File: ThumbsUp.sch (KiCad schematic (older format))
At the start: 165 parts, among them IC1 RP2040, IC2 W25Q128JVSIM, IC3 RP2040, IC4 W25Q128JVSIM, J1 Conn_01x04_Male, J10 Raiser_Male, J11 Raiser_Female, J12 Raiser_Male, J13 Raiser_Female, J14 Raiser_Male, J15 Raiser_Female, J16 Raiser_Male, J17 Raiser_Female, J18 Raiser_Male, J19 Raiser_Female, J2 Conn_01x04_Male, J20 Conn_01x04_Female, J21 Conn_01x04_Female, J22 Conn_01x04_Female, J23 Conn_01x04_Female, J24 Conn_01x04_Male, J25 Conn_01x04_Male, J26 Conn_01x04_Male, J27 Conn_01x04_Male, J28 Conn_01x04_Female, J29 Conn_01x04_Female, J3 Conn_01x04_Female, J30 Conn_01x04_Female, J31 Conn_01x04_Female, J32 USB_C_Receptacle_USB2.0, J33 Raiser_Male, J34 Raiser_Female, J35 Raiser_Male, J36 STX-3501-3N, J37 USB_C_Receptacle_USB2.0, J38 Raiser_Female, J39 Raiser_Male, J4 Conn_01x04_Male, J40 Raiser_Female, J41 Raiser_Male, J42 Raiser_Female, J43 Raiser_Male, J44 Raiser_Female, J45 Raiser_Male, J46 STX-3501-3N, J47 Raiser_Female, J48 Raiser_Male, J5 Conn_01x04_Female, J6 Conn_01x04_Male, J7 Conn_01x04_Male, J8 Conn_01x04_Male, J9 Raiser_Female, U1 NCP1117-3.3_SOT223, U2 NCP1117-3.3_SOT223, Y1 ABLS-12.000MHZ-B4-T, Y2 ABLS-12.000MHZ-B4-T

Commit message: Roughed in the lower plates
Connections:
- net K_0: now also J25.2 (Pin_2); no longer J25.3 (Pin_3)
- net K_1: now also J2.3 (Pin_3); no longer J2.2 (Pin_2)
- net K_2: now also J2.2 (Pin_2); no longer J2.3 (Pin_3)
- net K_3: now also J2.1 (Pin_1); no longer J2.4 (Pin_4)
- net K_8: now also J25.4 (Pin_4); no longer J25.1 (Pin_1)
- net K_9: now also J25.3 (Pin_3); no longer J25.2 (Pin_2)
- net K_DEL: now also J25.1 (Pin_1); no longer J25.4 (Pin_4)
- net K_GRAVE: now also J2.4 (Pin_4); no longer J2.1 (Pin_1)
- net at J21.1 (Pin_1): now also MX48.2 (ROW); no longer MX45.2 (ROW)
- net at J21.2 (Pin_2): now also MX47.2 (ROW); no longer MX46.2 (ROW)
- net at J21.3 (Pin_3): now also MX46.2 (ROW); no longer MX47.2 (ROW)
- net at J21.4 (Pin_4): now also MX45.2 (ROW); no longer MX48.2 (ROW)
- net at J29.1 (Pin_1): now also MX53.2 (ROW); no longer MX56.2 (ROW)
- net at J29.2 (Pin_2): now also MX54.2 (ROW); no longer MX55.2 (ROW)
- net at J29.3 (Pin_3): now also MX55.2 (ROW); no longer MX54.2 (ROW)
- net at J29.4 (Pin_4): now also MX56.2 (ROW); no longer MX53.2 (ROW)
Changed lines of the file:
@@
 L Connector:Conn_01x04_Male J2
 U 1 1 63651670
-P 6150 12300
-F 0 "J2" H 5950 12250 50  0000 L CNN
-F 1 "Conn_01x04_Male" V 6100 12000 50  0000 L CNN
-F 2 "Connector_PinHeader_2.54mm:PinHeader_1x04_P2.54mm_Vertical" H 6150 12300 50  0001 C CNN
-F 3 "~" H 6150 12300 50  0001 C CNN
-	1    6150 12300
-	1    0    0    1
+P 6150 12200
+F 0 "J2" H 5950 12150 50  0000 L CNN
+F 1 "Conn_01x04_Male" V 6100 11900 50  0000 L CNN
+F 2 "Connector_PinHeader_2.54mm:PinHeader_1x04_P2.54mm_Vertical" H 6150 12200 50  0001 C CNN
+F 3 "~" H 6150 12200 50  0001 C CNN
+	1    6150 12200
+	1    0    0    -1
 $EndComp
 $Comp
@@
 L Connector:Conn_01x04_Male J25
 U 1 1 636DA3F2
-P 12450 12250
-F 0 "J25" H 12250 12100 50  0000 L CNN
-F 1 "Conn_01x04_Male" V 12400 11950 50  0000 L CNN
-F 2 "Connector_PinHeader_2.54mm:PinHeader_1x04_P2.54mm_Vertical" H 12450 12250 50  0001 C CNN
-F 3 "~" H 12450 12250 50  0001 C CNN
-	1    12450 12250
-	-1   0    0    1
+P 12450 12150
+F 0 "J25" H 12250 12000 50  0000 L CNN
+F 1 "Conn_01x04_Male" V 12400 11850 50  0000 L CNN
+F 2 "Connector_PinHeader_2.54mm:PinHeader_1x04_P2.54mm_Vertical" H 12450 12150 50  0001 C CNN
+F 3 "~" H 12450 12150 50  0001 C CNN
+	1    12450 12150
+	-1   0    0    -1
 $EndComp
 $Comp
 L Connector:Conn_01x04_Female J29
 U 1 1 636DA3F8
-P 13000 12250
-F 0 "J29" H 13100 12200 50  0000 L CNN
-F 1 "Conn_01x04_Female" V 13050 11900 50  0000 L CNN
-F 2 "Connector_PinSocket_2.54mm:PinSocket_1x04_P2.54mm_Vertical" H 13000 12250 50  0001 C CNN
-F 3 "~" H 13000 12250 50  0001 C CNN
-	1    13000 12250
-	-1   0    0    1
+P 13000 12150
+F 0 "J29" H 13100 12100 50  0000 L CNN
+F 1 "Conn_01x04_Female" V 13050 11800 50  0000 L CNN
+F 2 "Connector_PinSocket_2.54mm:PinSocket_1x04_P2.54mm_Vertical" H 13000 12150 50  0001 C CNN
+F 3 "~" H 13000 12150 50  0001 C CNN
+	1    13000 12150
+	-1   0    0    -1
 $EndComp
 $Comp
@@
 L Connector:Conn_01x04_Female J21
 U 1 1 63650D67
-P 5600 12300
-F 0 "J21" H 5700 12250 50  0000 L CNN
-F 1 "Conn_01x04_Female" V 5650 11850 50  0000 L CNN
-F 2 "Connector_PinSocket_2.54mm:PinSocket_1x04_P2.54mm_Vertical" H 5600 12300 50  0001 C CNN
-F 3 "~" H 5600 12300 50  0001 C CNN
-	1    5600 12300
-	1    0    0    1
-$EndComp
-$Comp
+P 5600 12200
+F 0 "J21" H 5700 12150 50  0000 L CNN
+F 1 "Conn_01x04_Female" V 5650 11750 50  0000 L CNN
+F 2 "Connector_PinSocket_2.54mm:PinSocket_1x04_P2.54mm_Vertical" H 5600 12200 50  0001 C CNN
+F 3 "~" H 5600 12200 50  0001 C CNN
+	1    5600 12200
+	1    0    0    -1
+$EndComp
+$Comp

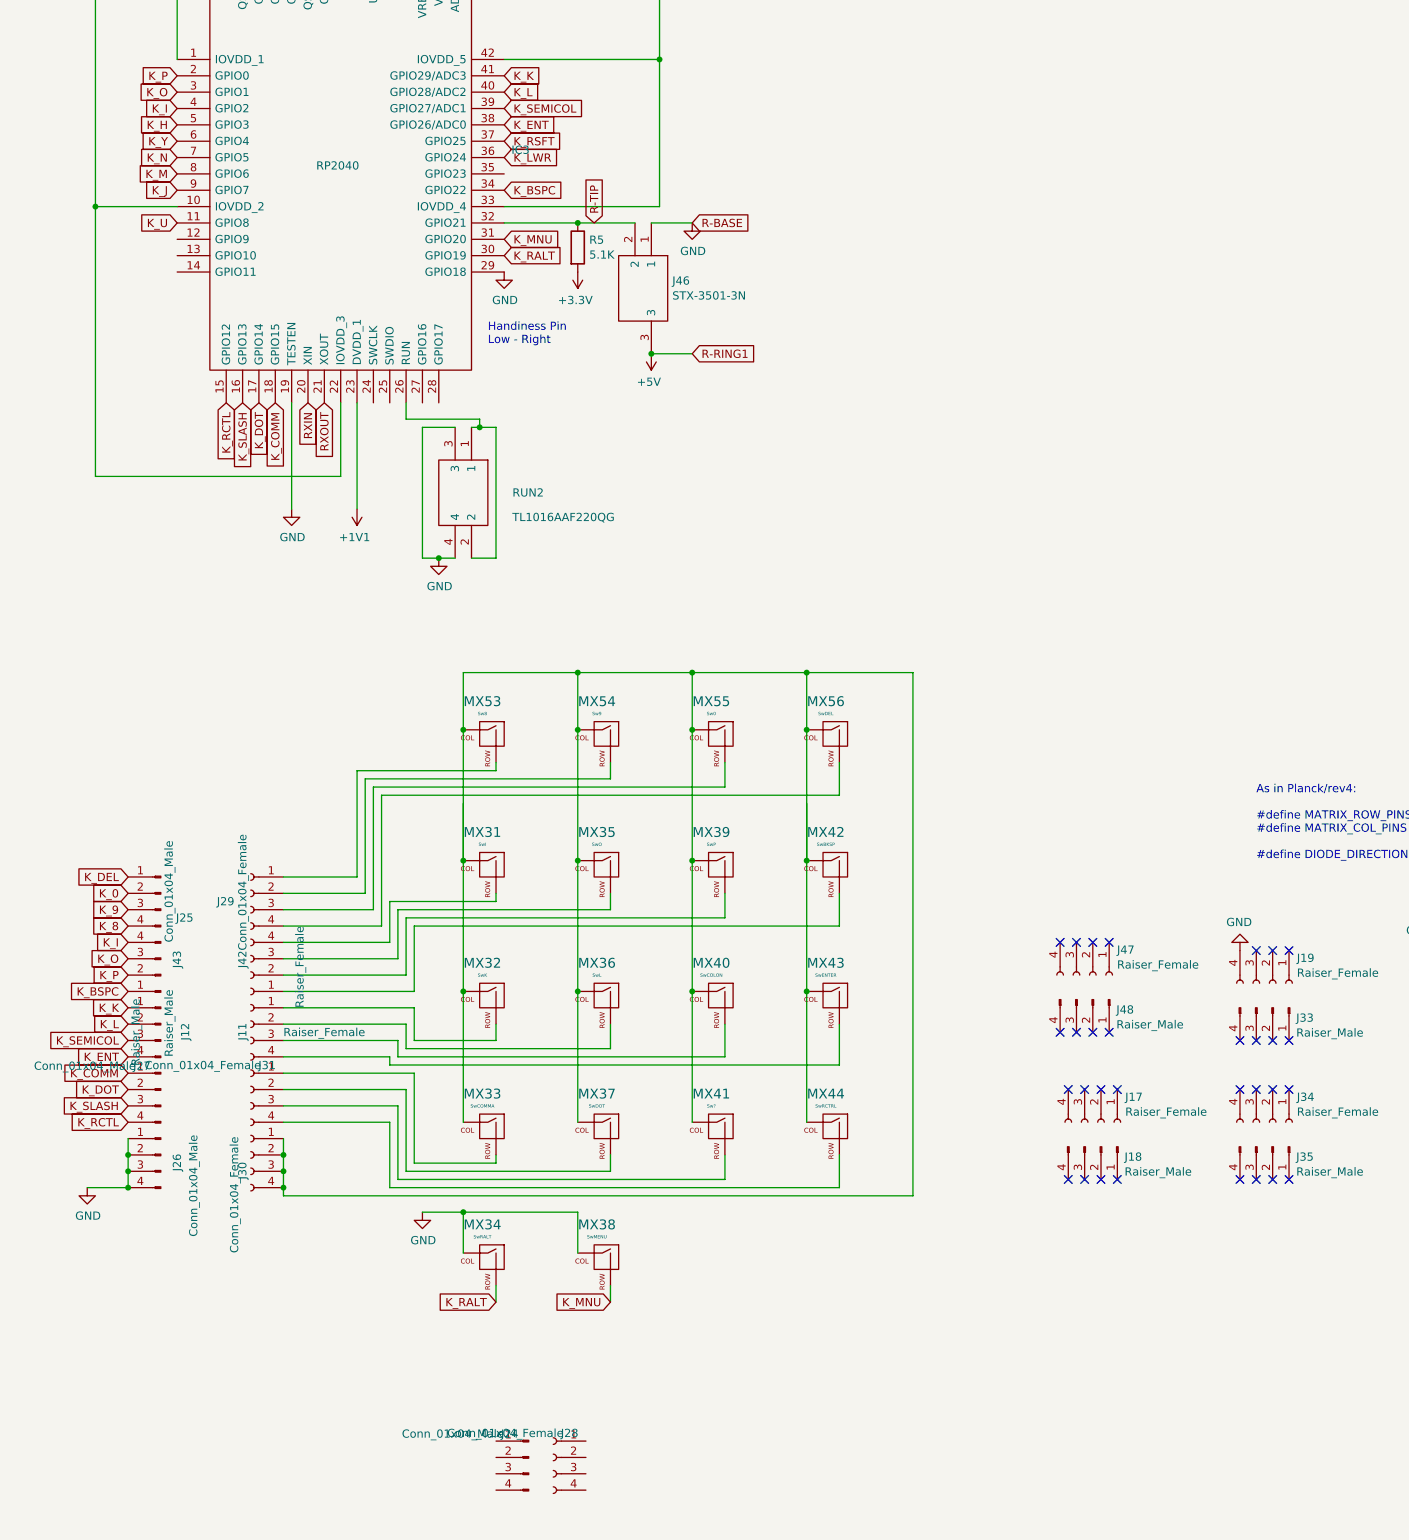
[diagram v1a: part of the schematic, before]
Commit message: Routed R2
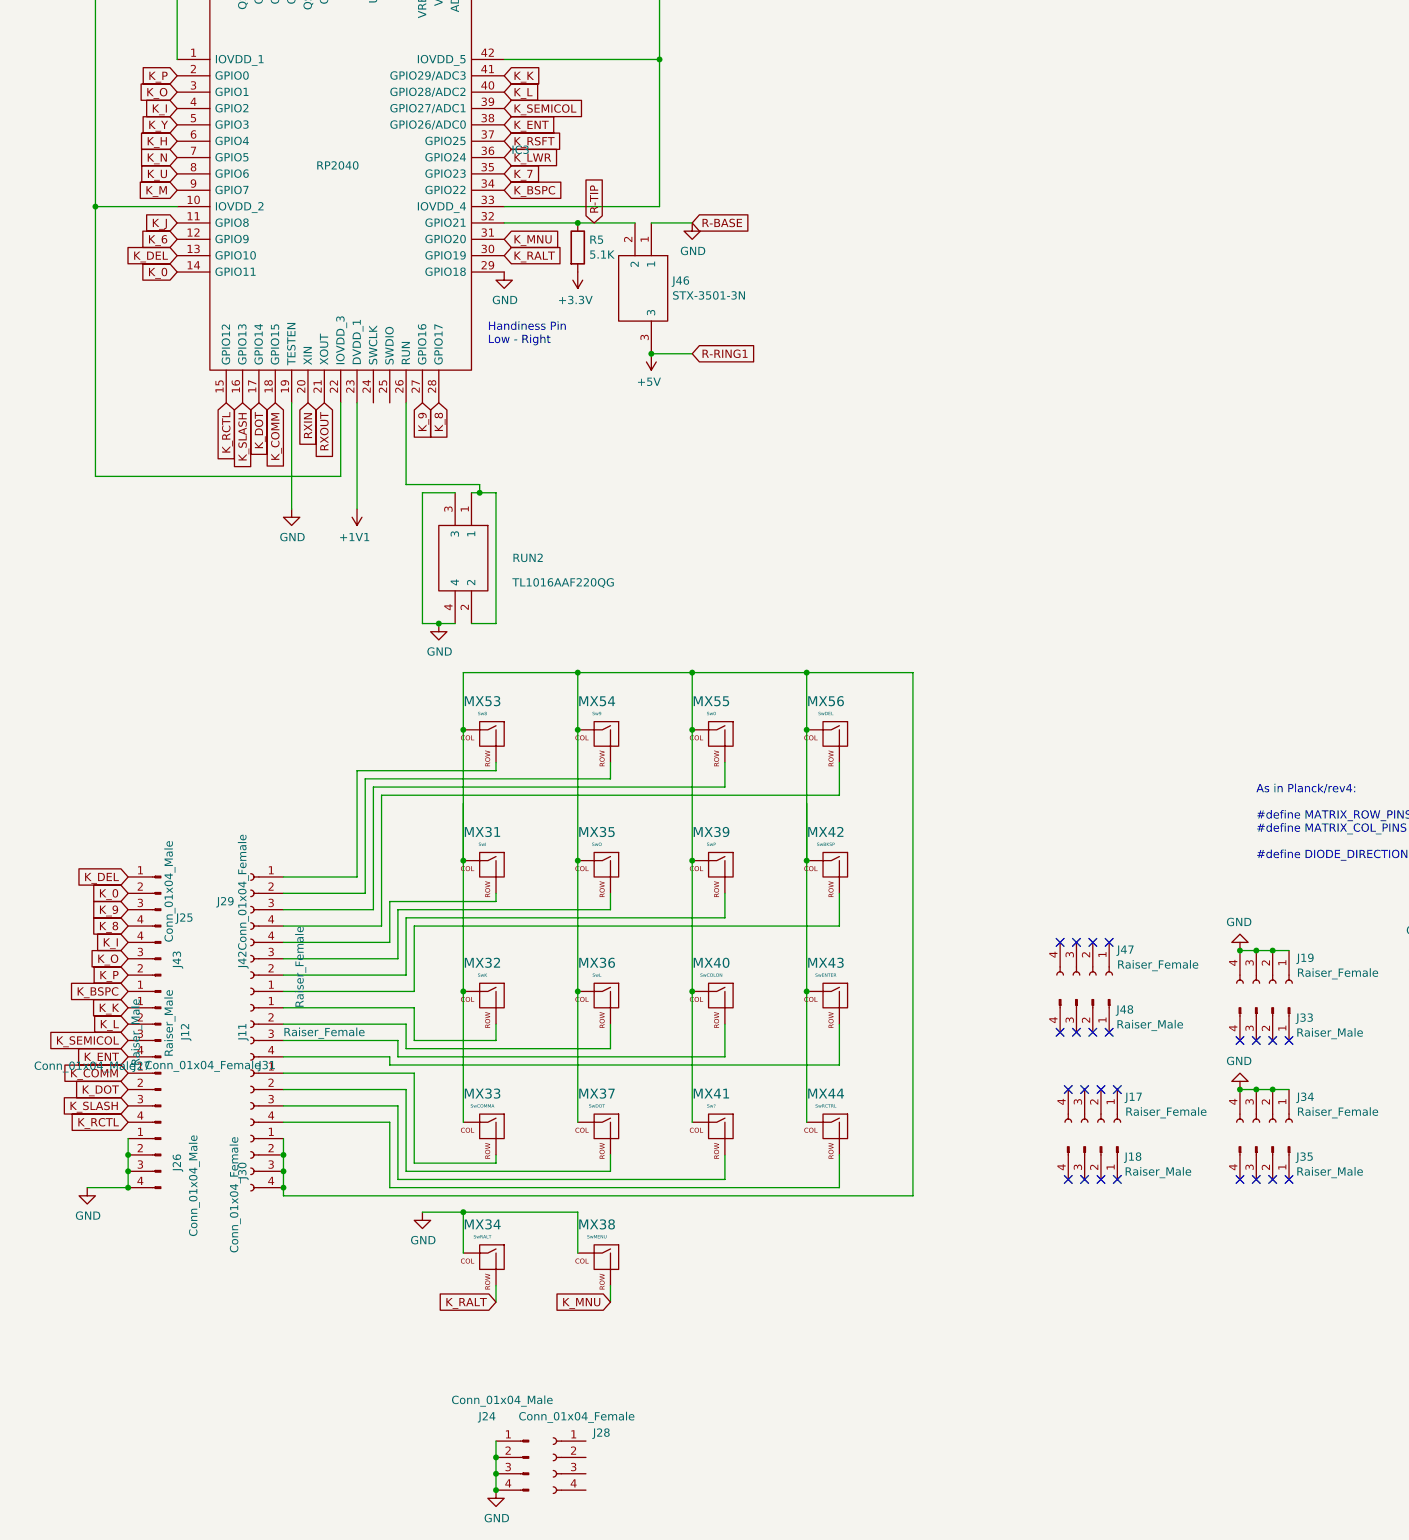
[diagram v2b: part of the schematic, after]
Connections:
- net GND: now also J19.1 (Pin_1), J19.2 (Pin_2), J19.3 (Pin_3), J24.1 (Pin_1), J24.2 (Pin_2), J24.3 (Pin_3), J24.4 (Pin_4), J34.1 (Pin_1), J34.2 (Pin_2), J34.3 (Pin_3), J34.4 (Pin_4)
- net K_0: now also IC3.14 (GPIO11)
- net K_6: now also IC3.12 (GPIO9)
- net K_7: now also IC3.35 (GPIO23)
- net K_8: now also IC3.28 (GPIO17)
- net K_9: now also IC3.27 (GPIO16)
- net K_DEL: now also IC3.13 (GPIO10)
- net K_H: now also IC3.6 (GPIO4); no longer IC3.5 (GPIO3)
- net K_J: now also IC3.11 (GPIO8); no longer IC3.9 (GPIO7)
- net K_M: now also IC3.9 (GPIO7); no longer IC3.8 (GPIO6)
- net K_U: now also IC3.8 (GPIO6); no longer IC3.11 (GPIO8)
- net K_Y: now also IC3.5 (GPIO3); no longer IC3.6 (GPIO4)
- no-connect marks 84 -> 77
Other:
- moved on the sheet: RUN2
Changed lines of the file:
@@
 U 1 1 636DA3E6
 P 14850 15600
-F 0 "J28" H 14696 15748 50  0000 L CNN
-F 1 "Conn_01x04_Female" H 14787 15748 50  0000 L CNN
+F 0 "J28" H 14500 15750 50  0000 L CNN
+F 1 "Conn_01x04_Female" H 14350 15850 50  0000 L CNN
 F 2 "Connector_PinSocket_2.54mm:PinSocket_1x04_P2.54mm_Vertical" H 14850 15600 50  0001 C CNN
 F 3 "~" H 14850 15600 50  0001 C CNN
@@
 	0    1    1    0
 $EndComp
-NoConn ~ 19050 13350
-NoConn ~ 19150 13350
-NoConn ~ 19250 13350
-NoConn ~ 19350 13350
 NoConn ~ 19050 13900
 NoConn ~ 19150 13900
@@
 	0    1    1    0
 $EndComp
-NoConn ~ 19150 12500
-NoConn ~ 19250 12500
-NoConn ~ 19350 12500
 NoConn ~ 19050 13050
 NoConn ~ 19150 13050
@@
 L power:GND #PWR0143
 U 1 1 63C338F1
-P 14150 10100
-F 0 "#PWR0143" H 14150 9850 50  0001 C CNN
-F 1 "GND" H 14155 9927 50  0000 C CNN
-F 2 "" H 14150 10100 50  0001 C CNN
-F 3 "" H 14150 10100 50  0001 C CNN
-	1    14150 10100
+P 14150 10500
+F 0 "#PWR0143" H 14150 10250 50  0001 C CNN
+F 1 "GND" H 14155 10327 50  0000 C CNN
+F 2 "" H 14150 10500 50  0001 C CNN
+F 3 "" H 14150 10500 50  0001 C CNN
+	1    14150 10500
 	1    0    0    -1
 $EndComp
@@
 L TL1016AAF220QG:TL1016AAF220QG RUN2
 U 1 1 63C33927
-P 14350 9300
-F 0 "RUN2" V 14750 9550 50  0000 L CNN
-F 1 "TL1016AAF220QG" V 14900 9550 50  0000 L CNN
-F 2 "TL1016AAF220QG:TL1016AAF220QG" H 15000 9400 50  0001 L CNN
-F 3 "https://eu.mouser.com/datasheet/2/140/E_Switch_05112022_TL1016_Datasheet-2943618.pdf" H 15000 9300 50  0001 L CNN
-F 4 "Tactile Switches Tactile Switch SPST OFF-(ON) 50mA 12VDC" H 15000 9200 50  0001 L CNN "Description"
-F 5 "1.35" H 15000 9100 50  0001 L CNN "Height"
-F 6 "E-Switch" H 15000 9000 50  0001 L CNN "Manufacturer_Name"
-F 7 "TL1016AAF220QG" H 15000 8900 50  0001 L CNN "Manufacturer_Part_Number"
-F 8 "612-TL1016AAF220QG" H 15000 8800 50  0001 L CNN "Mouser Part Number"
-F 9 "https://www.mouser.co.uk/ProductDetail/E-Switch/TL1016AAF220QG?qs=t7xnP681wgW5zrSpkWH91Q%3D%3D" H 15000 8700 50  0001 L CNN "Mouser Price/Stock"
-F 10 "" H 15000 8600 50  0001 L CNN "Arrow Part Number"
-F 11 "" H 15000 8500 50  0001 L CNN "Arrow Price/Stock"
-F 12 "" H 15000 8400 50  0001 L CNN "Mouser Testing Part Number"
-F 13 "" H 15000 8300 50  0001 L CNN "Mouser Testing Price/Stock"
-	1    14350 9300
+P 14350 9700
+F 0 "RUN2" V 14750 9950 50  0000 L CNN
+F 1 "TL1016AAF220QG" V 14900 9950 50  0000 L CNN
+F 2 "TL1016AAF220QG:TL1016AAF220QG" H 15000 9800 50  0001 L CNN
+F 3 "https://eu.mouser.com/datasheet/2/140/E_Switch_05112022_TL1016_Datasheet-2943618.pdf" H 15000 9700 50  0001 L CNN
+F 4 "Tactile Switches Tactile Switch SPST OFF-(ON) 50mA 12VDC" H 15000 9600 50  0001 L CNN "Description"
+F 5 "1.35" H 15000 9500 50  0001 L CNN "Height"
+F 6 "E-Switch" H 15000 9400 50  0001 L CNN "Manufacturer_Name"
+F 7 "TL1016AAF220QG" H 15000 9300 50  0001 L CNN "Manufacturer_Part_Number"
+F 8 "612-TL1016AAF220QG" H 15000 9200 50  0001 L CNN "Mouser Part Number"
+F 9 "https://www.mouser.co.uk/ProductDetail/E-Switch/TL1016AAF220QG?qs=t7xnP681wgW5zrSpkWH91Q%3D%3D" H 15000 9100 50  0001 L CNN "Mouser Price/Stock"
+F 10 "" H 15000 9000 50  0001 L CNN "Arrow Part Number"
+F 11 "" H 15000 8900 50  0001 L CNN "Arrow Price/Stock"
+F 12 "" H 15000 8800 50  0001 L CNN "Mouser Testing Part Number"
+F 13 "" H 15000 8700 50  0001 L CNN "Mouser Testing Price/Stock"
+	1    14350 9700
 	0    1    1    0
 $EndComp
 Wire Wire Line
-	14350 9300 14400 9300
+	14350 9700 14400 9700
 Wire Wire Line
-	14500 9300 14500 10100
+	14500 9700 14500 10500
 $Comp
 L TL1016AAF220QG:TL1016AAF220QG BOOTSEL2
@@
 U 1 1 636DA3EC
 P 14700 15600
-F 0 "J24" H 14762 15744 50  0000 L CNN
-F 1 "Conn_01x04_Male" H 14853 15744 50  0000 L CNN
+F 0 "J24" H 14900 15850 50  0000 L CNN
+F 1 "Conn_01x04_Male" H 14550 15950 50  0000 L CNN
 F 2 "Connector_PinHeader_2.54mm:PinHeader_1x04_P2.54mm_Vertical" H 14700 15600 50  0001 C CNN
 F 3 "~" H 14700 15600 50  0001 C CNN
@@
 Text GLabel 12550 7350 0    50   Input ~ 0
 K_I
-Text GLabel 12550 7450 0    50   Input ~ 0
-K_H
 Text GLabel 12550 7550 0    50   Input ~ 0
+K_H
+Text GLabel 12550 7450 0    50   Input ~ 0
 K_Y
 Text GLabel 12550 7650 0    50   Input ~ 0
 K_N
-Text GLabel 12550 7750 0    50   Input ~ 0
-K_M
 Text GLabel 12550 7850 0    50   Input ~ 0
-K_J
+K_M
 Text GLabel 12550 8050 0    50   Input ~ 0
+K_J
+Text GLabel 12550 7750 0    50   Input ~ 0
 K_U
 Wire Wire Line
-	14050 10100 14150 10100
+	14050 10500 14150 10500
 Wire Wire Line
-	14050 9300 14250 9300
+	14050 9700 14250 9700
 Wire Wire Line
-	14050 10100 14050 9300
+	14050 10500 14050 9700
 Wire Wire Line
 	3650 9200 3650 9300
@@
 	4050 10150 4200 10150
 Wire Wire Line
-	13950 9150 13950 9250
-Wire Wire Line
-	13950 9250 14400 9250
+	13950 9650 14400 9650
 Wire Wire Line
-	14400 9250 14400 9300
-Connection ~ 14400 9300
+	14400 9650 14400 9700
+Connection ~ 14400 9700
 Wire Wire Line
-	14400 9300 14500 9300
-Connection ~ 14150 10100
+	14400 9700 14500 9700
+Connection ~ 14150 10500
 Wire Wire Line
-	14150 10100 14250 10100
+	14150 10500 14250 10500
 Wire Wire Line
-	14350 10100 14500 10100
+	14350 10500 14500 10500
 Text GLabel 4250 7200 2    50   Input ~ 0
 K_LSFT
@@
 Text GLabel 12250 12050 0    50   Input ~ 0
 K_DEL
+Text GLabel 12550 8150 0    50   Input ~ 0
+K_6
+Text GLabel 12550 8250 0    50   Input ~ 0
+K_DEL
+Text GLabel 12550 8350 0    50   Input ~ 0
+K_0
+Wire Wire Line
+	13950 9150 13950 9650
+Text GLabel 14050 9150 3    50   Input ~ 0
+K_9
+Text GLabel 14150 9150 3    50   Input ~ 0
+K_8
+Text GLabel 14550 7750 2    50   Input ~ 0
+K_7
+Wire Wire Line
+	19050 13350 19150 13350
+Connection ~ 19150 13350
+Wire Wire Line
+	19150 13350 19250 13350
+Connection ~ 19250 13350
+Wire Wire Line
+	19250 13350 19350 13350
+$Comp
+L power:GND #PWR0159
+U 1 1 6417F56E
+P 19050 13350
+F 0 "#PWR0159" H 19050 13100 50  0001 C CNN
+F 1 "GND" H 19055 13177 50  0000 C CNN
+F 2 "" H 19050 13350 50  0001 C CNN
+F 3 "" H 19050 13350 50  0001 C CNN
+	1    19050 13350
+	-1   0    0    1
+$EndComp
+Connection ~ 19050 13350
+Wire Wire Line
+	19350 12500 19250 12500
+Connection ~ 19050 12500
+Connection ~ 19150 12500
+Wire Wire Line
+	19150 12500 19050 12500
+Connection ~ 19250 12500
+Wire Wire Line
+	19250 12500 19150 12500
+Wire Wire Line
+	14500 15500 14500 15600
+Connection ~ 14500 15600
+Wire Wire Line
+	14500 15600 14500 15700
+Connection ~ 14500 15700
+Wire Wire Line
+	14500 15700 14500 15800
+$Comp
+L power:GND #PWR?
+U 1 1 642F3305
+P 14500 15800
+F 0 "#PWR?" H 14500 15550 50  0001 C CNN
+F 1 "GND" H 14505 15627 50  0000 C CNN
+F 2 "" H 14500 15800 50  0001 C CNN
+F 3 "" H 14500 15800 50  0001 C CNN
+	1    14500 15800
+	1    0    0    -1
+$EndComp
+Connection ~ 14500 15800
 $EndSCHEMATC

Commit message: Routing L2
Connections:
- net K_C: now also IC1.5 (GPIO3); no longer IC1.8 (GPIO6)
- net K_LCTL: now also IC1.8 (GPIO6); no longer IC1.5 (GPIO3)
- net K_WIN: now also J1.1 (Pin_1)
- net K_X: now also IC1.6 (GPIO4); no longer IC1.7 (GPIO5)
- net K_Z: now also IC1.7 (GPIO5); no longer IC1.6 (GPIO4)
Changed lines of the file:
@@
 Text GLabel 13150 9150 3    50   Input ~ 0
 K_COMM
+Text GLabel 2250 7800 0    50   Input ~ 0
+K_LCTL
+Text GLabel 2250 7700 0    50   Input ~ 0
+K_Z
+Text GLabel 2250 7600 0    50   Input ~ 0
+K_X
 Text GLabel 2250 7500 0    50   Input ~ 0
-K_LCTL
-Text GLabel 2250 7600 0    50   Input ~ 0
-K_Z
-Text GLabel 2250 7700 0    50   Input ~ 0
-K_X
-Text GLabel 2250 7800 0    50   Input ~ 0
 K_C
 $Comp
@@
 	14500 15700 14500 15800
 $Comp
-L power:GND #PWR?
+L power:GND #PWR0160
 U 1 1 642F3305
 P 14500 15800
-F 0 "#PWR?" H 14500 15550 50  0001 C CNN
+F 0 "#PWR0160" H 14500 15550 50  0001 C CNN
 F 1 "GND" H 14505 15627 50  0000 C CNN
 F 2 "" H 14500 15800 50  0001 C CNN
@@
 $EndComp
 Connection ~ 14500 15800
+Text GLabel 5600 15050 2    50   Input ~ 0
+K_WIN
 $EndSCHEMATC
